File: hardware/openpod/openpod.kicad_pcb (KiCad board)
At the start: 2 copper layers, 65 x 90 mm, 18 parts

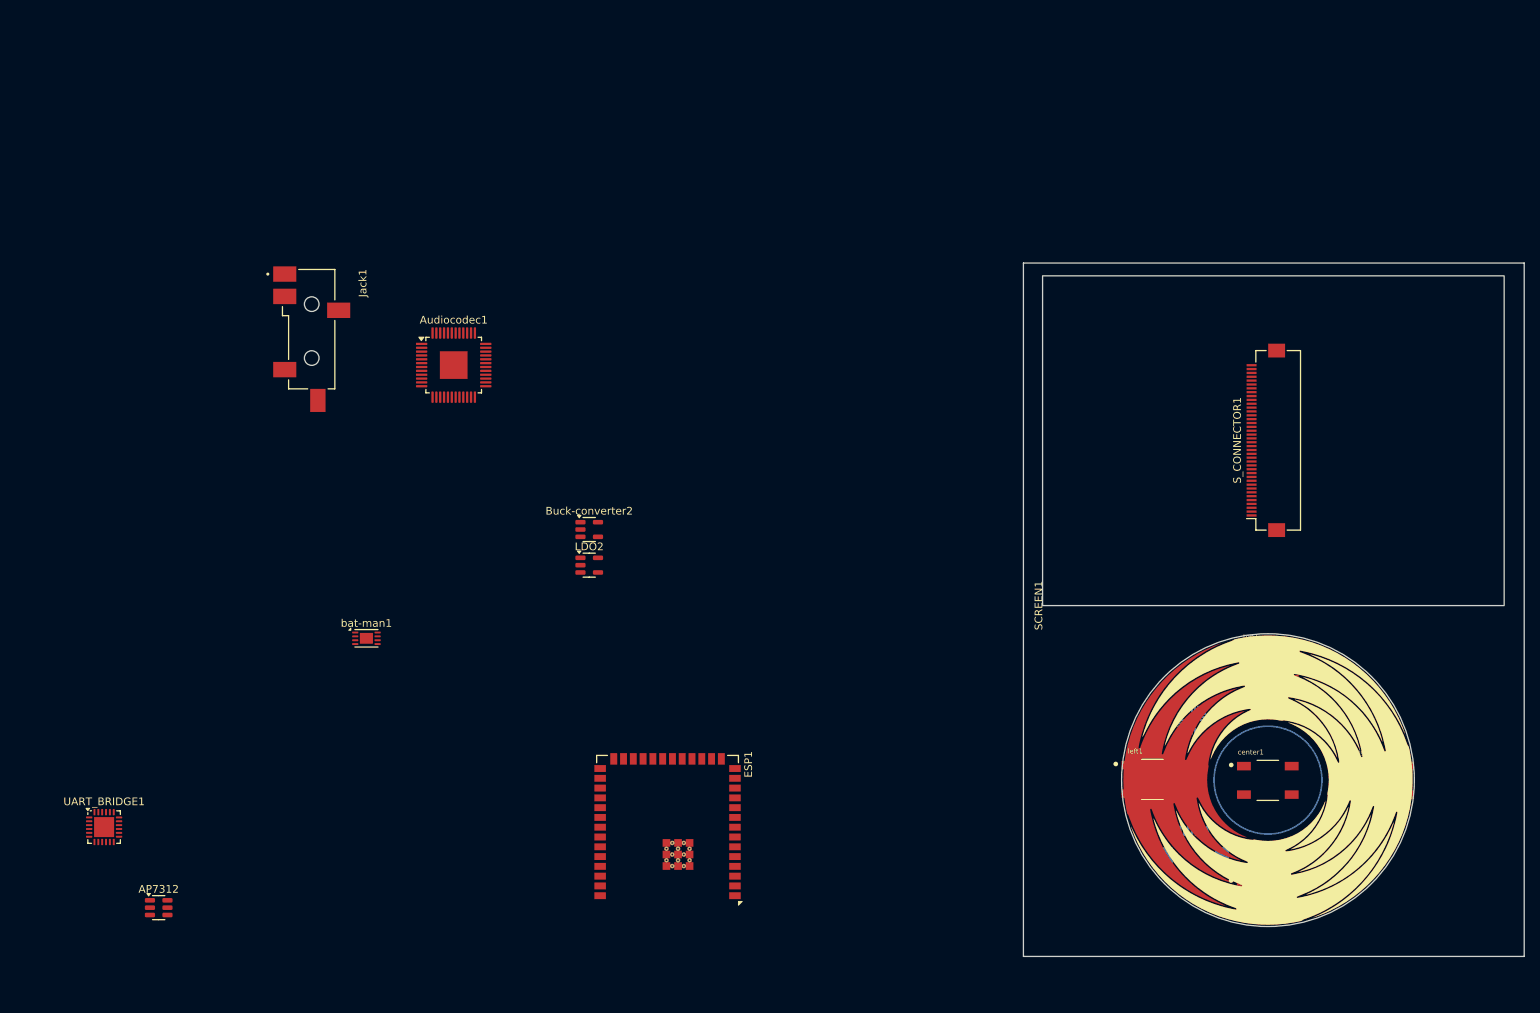
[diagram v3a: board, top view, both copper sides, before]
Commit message: added bluetooth
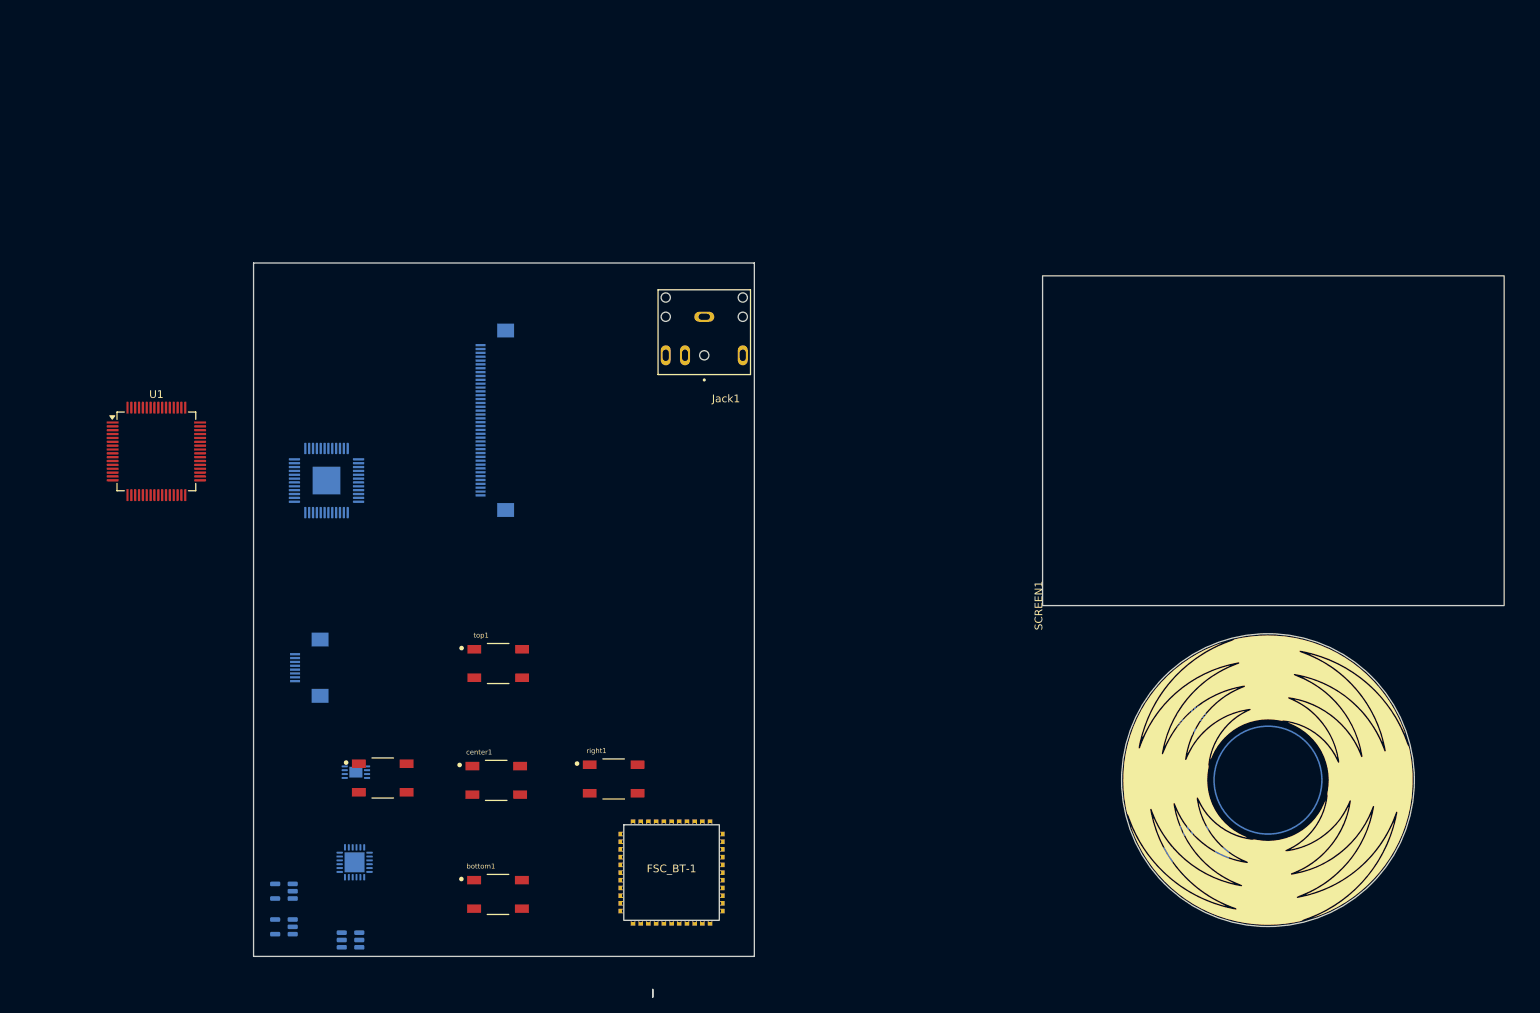
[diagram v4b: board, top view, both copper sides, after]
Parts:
- removed ESP1: ESP32-S3-WROOM-2, RF_Module:ESP32-S3-WROOM-2
- added FSC_BT-1: ~, openpod:fsc-bt1046, F.Cu at (154.3, 129.1)
- added U1: STM32F446RCTx, Package_QFP:LQFP-64_10x10mm_P0.5mm, F.Cu at (87.5, 74.5)
- added clickwheel-connector2: ~, Connector_FFC-FPC:Hirose_FH12-8S-0.5SH_1x08-1MP_P0.50mm_Horizontal, B.Cu at (107.3, 102.5)
- AP7312, Audiocodec1, Buck-converter2, LDO2, S_CONNECTOR1, UART_BRIDGE1, bat-man1: moved to B.Cu
- Jack1: value SJ-43515TS-SMT-TR -> SJ1-3524NG; footprint jack:CUI_SJ-43515TS-SMT-TR -> openpod:CUI_SJ1-3524NG
- moved center1 100.2 mm to (131.6, 117.1)
- moved S_CONNECTOR1 100.1 mm to (131.4, 70.4), turned to -90 degrees
- moved top1 99.9 mm to (131.8, 102.0)
- moved bottom1 99.9 mm to (131.8, 132.0)
- moved left1 99.9 mm to (116.8, 116.8)
- moved right1 99.9 mm to (146.8, 117.0)
- moved Buck-converter2 61.4 mm to (104.0, 131.5), turned to 180 degrees
- moved LDO2 61.4 mm to (104.0, 136.2), turned to 180 degrees
- moved Jack1 54.7 mm to (158.6, 57.0), turned to 180 degrees
- moved UART_BRIDGE1 32.8 mm to (113.2, 127.8), turned to 180 degrees
- moved AP7312 25.2 mm to (112.7, 137.9), turned to 180 degrees
- moved Audiocodec1 22.3 mm to (109.5, 78.2), turned to 180 degrees
- moved bat-man1 17.4 mm to (113.4, 116.1), turned to 180 degrees
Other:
- board size 65 x 90 mm -> 65 x 95.3 mm
